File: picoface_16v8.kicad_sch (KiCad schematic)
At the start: 23 parts, among them J1 ZX_Spectrum_Connector_48K_SOR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, J2 DE9_Plug, Q1 DMG2305, SW1 SW_USER, SW2 SW_RESET, SW3 SW_RUN, U2 Pico, U3 74LS240

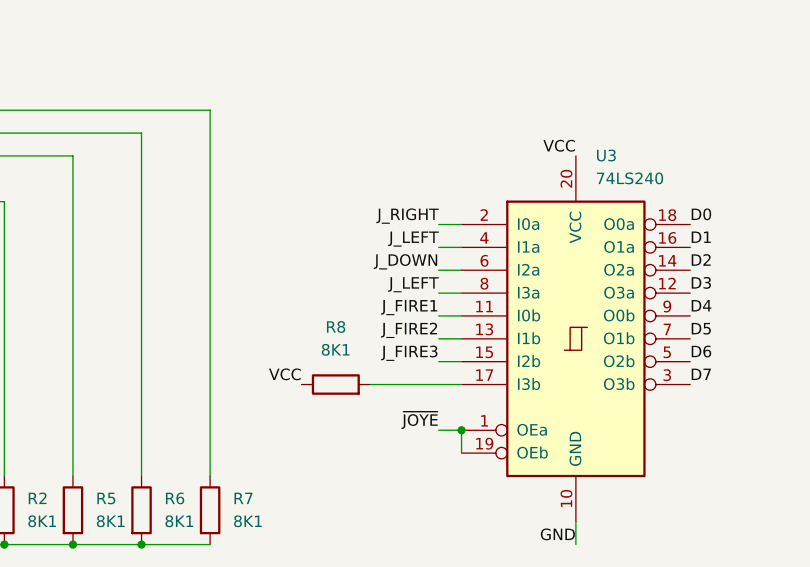
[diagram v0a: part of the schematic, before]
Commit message: Prototype B board, fix up mistakes in prototype A
Correct the joystick up connection, make SD card drill holes slightly larger.
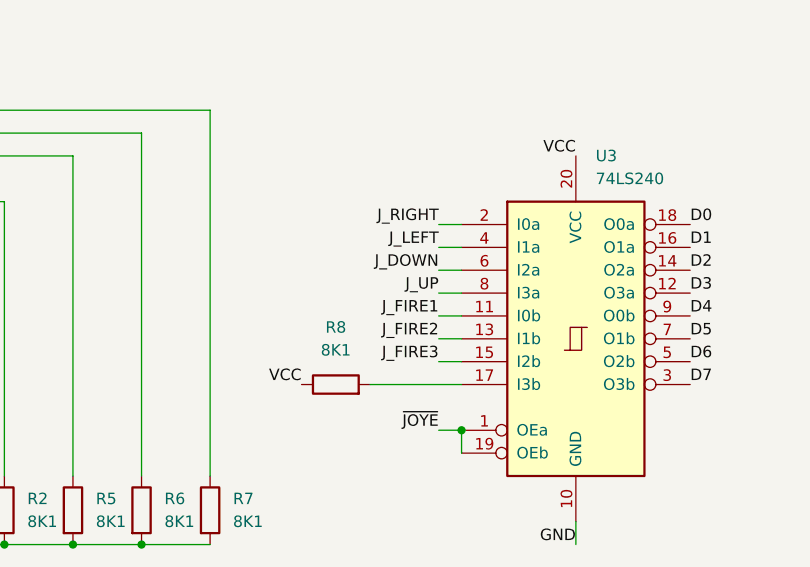
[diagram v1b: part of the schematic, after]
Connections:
- net J_LEFT: no longer U3.8 (I3a)
- net J_UP: now also U3.8 (I3a)
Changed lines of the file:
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@@
-		)
-	)
-	(label "J_LEFT"
-		(at 130.81 152.4 180)
-		(fields_autoplaced yes)
-		(effects
-			(font
-				(size 1.27 1.27)
-			)
-			(justify right bottom)
 		)
 	)
@@
 		(fields_autoplaced yes)
 		(effects
+			(font
+				(size 1.27 1.27)
+			)
+			(justify right bottom)
+		)
+	)
+	(label "J_UP"
+		(at 130.81 152.4 180)
+		(fields_autoplaced yes)
+		(effects

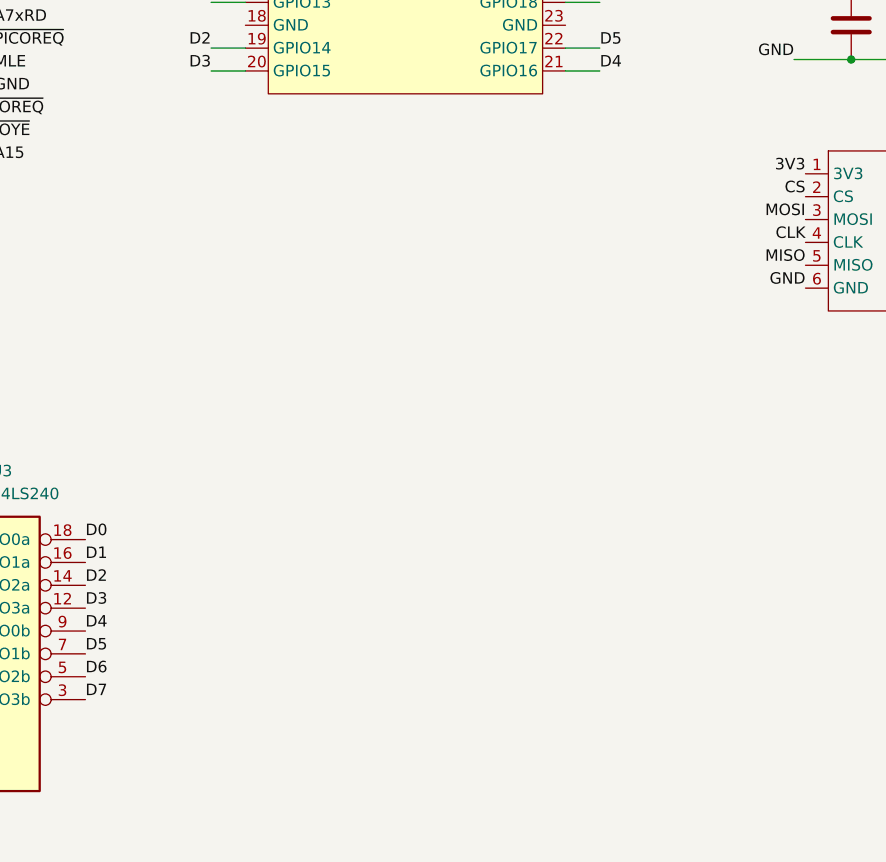
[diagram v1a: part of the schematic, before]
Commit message: Prototype B with pico ultimate pinout
Has two set of pads for the different types of pico.
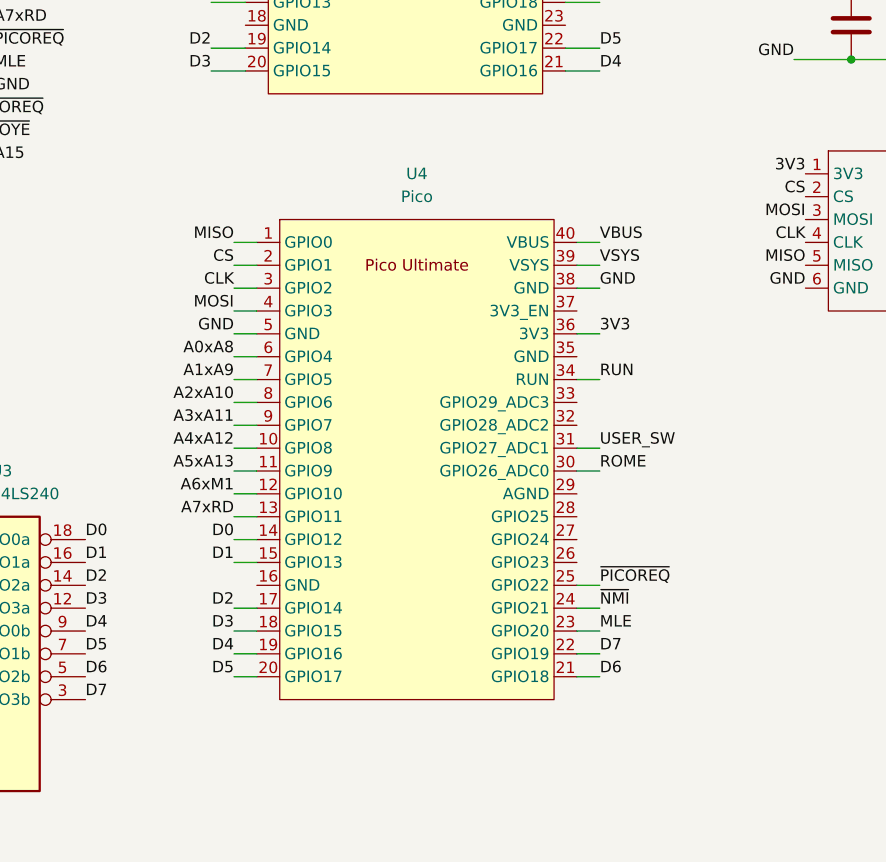
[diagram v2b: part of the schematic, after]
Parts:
- added U4: Pico, mysyms:RPi_Pico_SMD_TH_BA2, symbol mysyms:PicoUltimate
- U2: footprint mysyms:RPi_Pico_SMD_TH_BA -> mysyms:RPi_Pico_SMD_TH_BA2
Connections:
- net 3V3: now also U4.36 (3V3)
- net A0xA8: now also U4.6 (GPIO4)
- net A1xA9: now also U4.7 (GPIO5)
- net A2xA10: now also U4.8 (GPIO6)
- net A3xA11: now also U4.9 (GPIO7)
- net A4xA12: now also U4.10 (GPIO8)
- net A5xA13: now also U4.11 (GPIO9)
- net A6xM1: now also U4.12 (GPIO10)
- net A7xRD: now also U4.13 (GPIO11)
- net CLK: now also U4.3 (GPIO2)
- net CS: now also U4.2 (GPIO1)
- net D0: now also U4.14 (GPIO12)
- net D1: now also U4.15 (GPIO13)
- net D2: now also U4.17 (GPIO14)
- net D3: now also U4.18 (GPIO15)
- net D4: now also U4.19 (GPIO16)
- net D5: now also U4.20 (GPIO17)
- net D6: now also U4.21 (GPIO18)
- net D7: now also U4.22 (GPIO19)
- net GND: now also U4.38 (GND), U4.5 (GND)
- net MISO: now also U4.1 (GPIO0)
- net MLE: now also U4.23 (GPIO20)
- net MOSI: now also U4.4 (GPIO3)
- net ROME: now also U4.30 (GPIO26_ADC0)
- net RUN: now also U4.34 (RUN)
- net USER_SW: now also U4.31 (GPIO27_ADC1)
- net VBUS: now also U4.40 (VBUS)
- net VSYS: now also U4.39 (VSYS)
- net ~{NMI}: now also U4.24 (GPIO21)
- net ~{PICOREQ}: now also U4.25 (GPIO22)
